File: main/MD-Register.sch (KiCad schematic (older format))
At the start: 19 parts, among them U68 74LS245, U69 74LS173, U70 74LS173

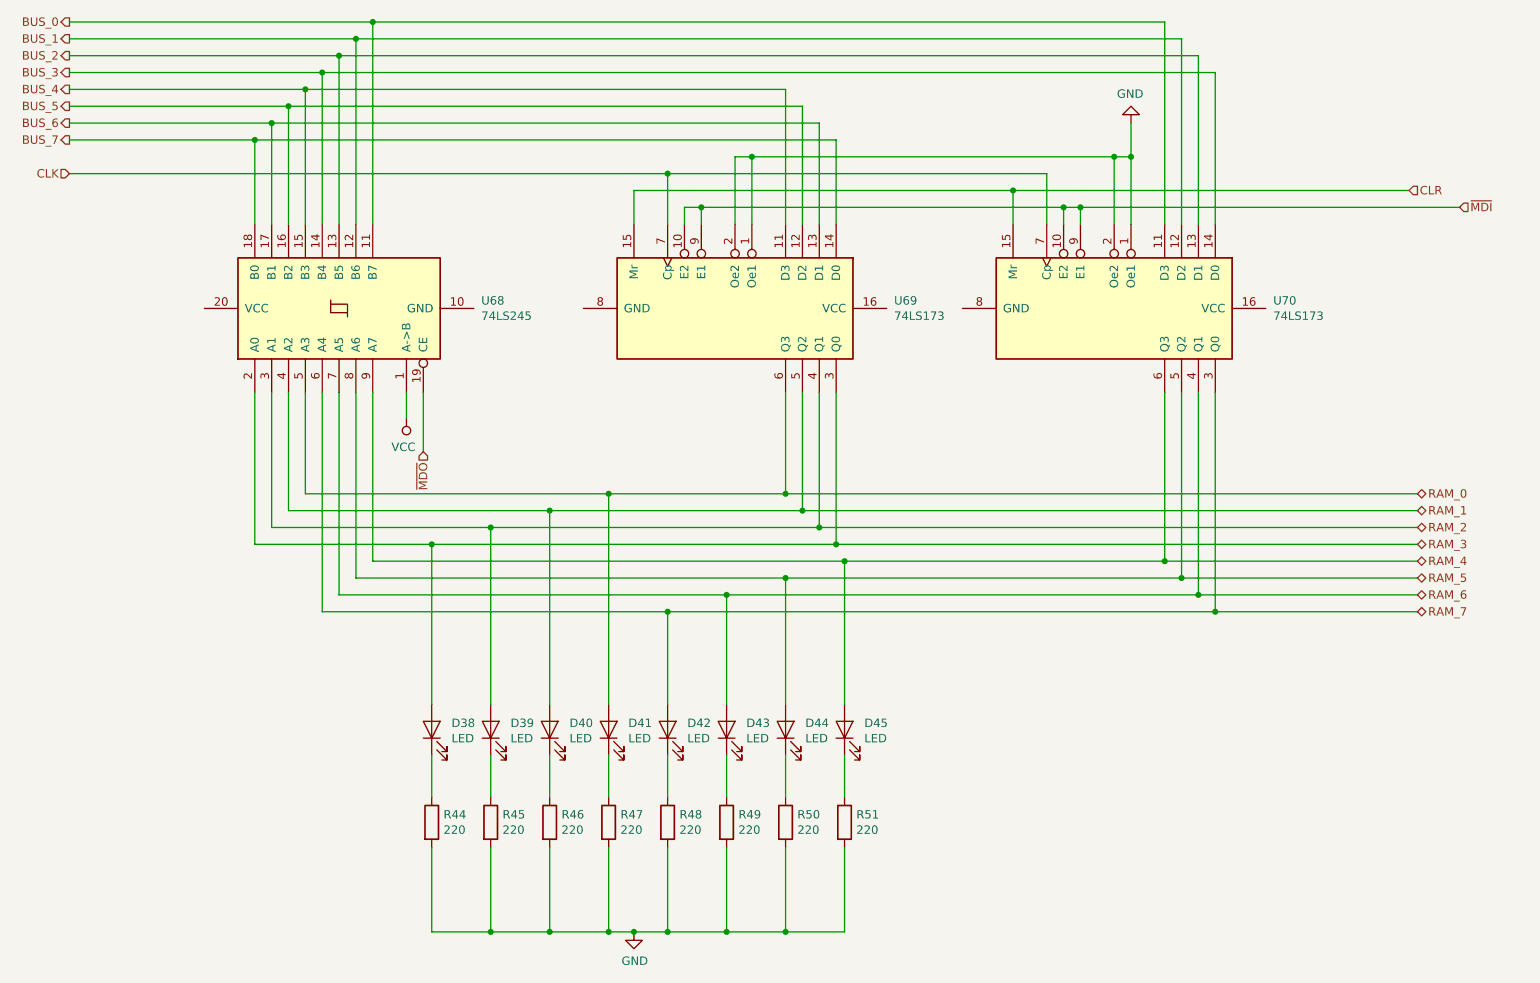
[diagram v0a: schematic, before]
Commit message: Replot main with symbols
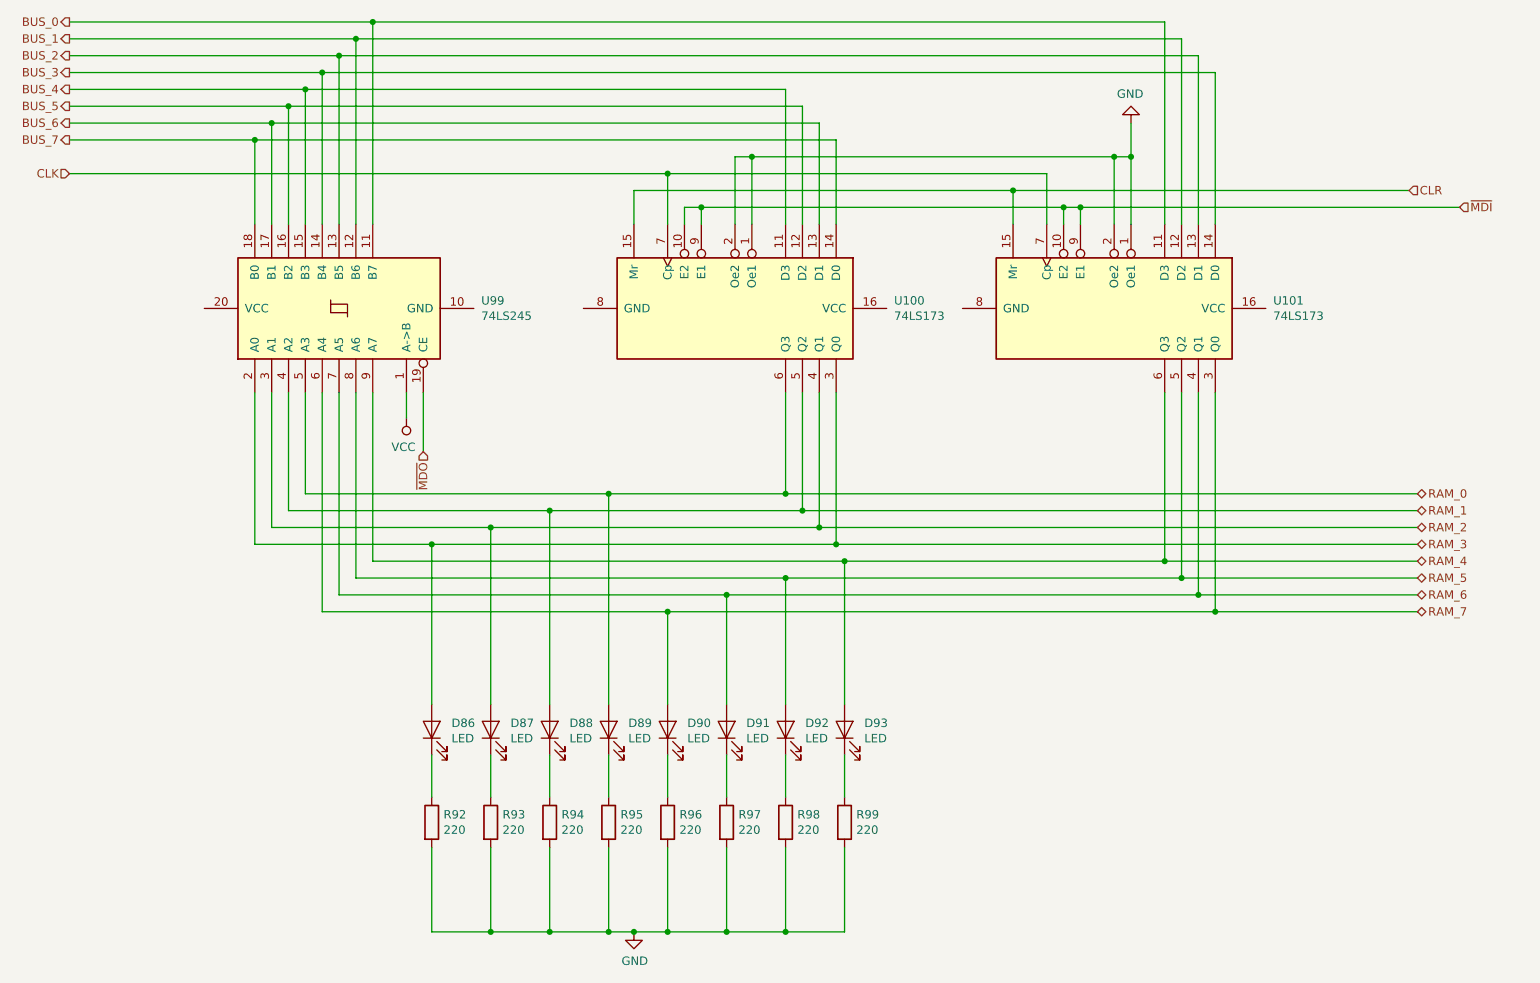
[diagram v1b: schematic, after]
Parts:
- renumbered D38 to D86, D39 to D87, D40 to D88, D41 to D89, D42 to D90, D43 to D91, D44 to D92, D45 to D93, R44 to R92, R45 to R93, R46 to R94, R47 to R95, R48 to R96, R49 to R97, R50 to R98, R51 to R99, U69 to U100, U70 to U101, U68 to U99
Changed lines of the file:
@@
 Sheet 26 26
 Title "Memory Data Register"
-Date "2019-11-13"
+Date "2019-11-17"
 Rev "v1.0"
 Comp "Christopher Milan"
@@
 AR Path="/5DA98D6D/5DA9A5B3/5E61466D" Ref="U?"  Part="1"
 AR Path="/5DA9B7A7/5E61466D" Ref="U?"  Part="1"
-AR Path="/5E5B2276/5D8079E9/5E61466D" Ref="U68"  Part="1"
-F 0 "U68" V 2746 2056 50  0000 R CNN
+AR Path="/5E5B2276/5D8079E9/5E61466D" Ref="U99"  Part="1"
+F 0 "U99" V 2746 2056 50  0000 R CNN
 F 1 "74LS245" V 2655 2056 50  0000 R CNN
 F 2 "" H 2700 2900 50  0001 C CNN
@@
 AR Path="/5DA98D6D/5DA9A5B3/5E61469A" Ref="U?"  Part="1"
 AR Path="/5DA9B7A7/5E61469A" Ref="U?"  Part="1"
-AR Path="/5E5B2276/5D8079E9/5E61469A" Ref="U70"  Part="1"
-F 0 "U70" V 7254 3844 50  0000 L CNN
+AR Path="/5E5B2276/5D8079E9/5E61469A" Ref="U101"  Part="1"
+F 0 "U101" V 7254 3844 50  0000 L CNN
 F 1 "74LS173" V 7345 3844 50  0000 L CNN
 F 2 "" H 7300 2900 50  0001 C CNN
@@
 AR Path="/5DA98D6D/5DA9A5B3/5E6146C4" Ref="D?"  Part="1"
 AR Path="/5DA9B7A7/5E6146C4" Ref="D?"  Part="1"
-AR Path="/5E5B2276/5D8079E9/5E6146C4" Ref="D38"  Part="1"
-F 0 "D38" V 3289 5283 50  0000 R CNN
+AR Path="/5E5B2276/5D8079E9/5E6146C4" Ref="D86"  Part="1"
+F 0 "D86" V 3289 5283 50  0000 R CNN
 F 1 "LED" V 3198 5283 50  0000 R CNN
 F 2 "" H 3250 5400 50  0001 C CNN
@@
 AR Path="/5DA98D6D/5DA9A5B3/5E6146CA" Ref="D?"  Part="1"
 AR Path="/5DA9B7A7/5E6146CA" Ref="D?"  Part="1"
-AR Path="/5E5B2276/5D8079E9/5E6146CA" Ref="D39"  Part="1"
-F 0 "D39" V 3639 5283 50  0000 R CNN
+AR Path="/5E5B2276/5D8079E9/5E6146CA" Ref="D87"  Part="1"
+F 0 "D87" V 3639 5283 50  0000 R CNN
 F 1 "LED" V 3548 5283 50  0000 R CNN
 F 2 "" H 3600 5400 50  0001 C CNN
@@
 AR Path="/5DA98D6D/5DA9A5B3/5E6146D0" Ref="D?"  Part="1"
 AR Path="/5DA9B7A7/5E6146D0" Ref="D?"  Part="1"
-AR Path="/5E5B2276/5D8079E9/5E6146D0" Ref="D40"  Part="1"
-F 0 "D40" V 3989 5283 50  0000 R CNN
+AR Path="/5E5B2276/5D8079E9/5E6146D0" Ref="D88"  Part="1"
+F 0 "D88" V 3989 5283 50  0000 R CNN
 F 1 "LED" V 3898 5283 50  0000 R CNN
 F 2 "" H 3950 5400 50  0001 C CNN
@@
 AR Path="/5DA98D6D/5DA9A5B3/5E6146D6" Ref="D?"  Part="1"
 AR Path="/5DA9B7A7/5E6146D6" Ref="D?"  Part="1"
-AR Path="/5E5B2276/5D8079E9/5E6146D6" Ref="D41"  Part="1"
-F 0 "D41" V 4339 5283 50  0000 R CNN
+AR Path="/5E5B2276/5D8079E9/5E6146D6" Ref="D89"  Part="1"
+F 0 "D89" V 4339 5283 50  0000 R CNN
 F 1 "LED" V 4248 5283 50  0000 R CNN
 F 2 "" H 4300 5400 50  0001 C CNN
@@
 AR Path="/5DA98D6D/5DA9A5B3/5E6146DC" Ref="D?"  Part="1"
 AR Path="/5DA9B7A7/5E6146DC" Ref="D?"  Part="1"
-AR Path="/5E5B2276/5D8079E9/5E6146DC" Ref="D42"  Part="1"
-F 0 "D42" V 4689 5283 50  0000 R CNN
+AR Path="/5E5B2276/5D8079E9/5E6146DC" Ref="D90"  Part="1"
+F 0 "D90" V 4689 5283 50  0000 R CNN
 F 1 "LED" V 4598 5283 50  0000 R CNN
 F 2 "" H 4650 5400 50  0001 C CNN
@@
 AR Path="/5DA98D6D/5DA9A5B3/5E6146E2" Ref="D?"  Part="1"
 AR Path="/5DA9B7A7/5E6146E2" Ref="D?"  Part="1"
-AR Path="/5E5B2276/5D8079E9/5E6146E2" Ref="D43"  Part="1"
-F 0 "D43" V 5039 5283 50  0000 R CNN
+AR Path="/5E5B2276/5D8079E9/5E6146E2" Ref="D91"  Part="1"
+F 0 "D91" V 5039 5283 50  0000 R CNN
 F 1 "LED" V 4948 5283 50  0000 R CNN
 F 2 "" H 5000 5400 50  0001 C CNN
@@
 AR Path="/5DA98D6D/5DA9A5B3/5E6146E8" Ref="D?"  Part="1"
 AR Path="/5DA9B7A7/5E6146E8" Ref="D?"  Part="1"
-AR Path="/5E5B2276/5D8079E9/5E6146E8" Ref="D44"  Part="1"
-F 0 "D44" V 5389 5283 50  0000 R CNN
+AR Path="/5E5B2276/5D8079E9/5E6146E8" Ref="D92"  Part="1"
+F 0 "D92" V 5389 5283 50  0000 R CNN
 F 1 "LED" V 5298 5283 50  0000 R CNN
 F 2 "" H 5350 5400 50  0001 C CNN
@@
 AR Path="/5DA98D6D/5DA9A5B3/5E6146EE" Ref="D?"  Part="1"
 AR Path="/5DA9B7A7/5E6146EE" Ref="D?"  Part="1"
-AR Path="/5E5B2276/5D8079E9/5E6146EE" Ref="D45"  Part="1"
-F 0 "D45" V 5739 5283 50  0000 R CNN
+AR Path="/5E5B2276/5D8079E9/5E6146EE" Ref="D93"  Part="1"
+F 0 "D93" V 5739 5283 50  0000 R CNN
 F 1 "LED" V 5648 5283 50  0000 R CNN
 F 2 "" H 5700 5400 50  0001 C CNN
@@
 AR Path="/5DA98D6D/5DA9A5B3/5E61470A" Ref="R?"  Part="1"
 AR Path="/5DA9B7A7/5E61470A" Ref="R?"  Part="1"
-AR Path="/5E5B2276/5D8079E9/5E61470A" Ref="R44"  Part="1"
-F 0 "R44" H 3320 5996 50  0000 L CNN
+AR Path="/5E5B2276/5D8079E9/5E61470A" Ref="R92"  Part="1"
+F 0 "R92" H 3320 5996 50  0000 L CNN
 F 1 "220" H 3320 5905 50  0000 L CNN
 F 2 "" V 3180 5950 50  0001 C CNN
@@
 AR Path="/5DA98D6D/5DA9A5B3/5E614710" Ref="R?"  Part="1"
 AR Path="/5DA9B7A7/5E614710" Ref="R?"  Part="1"
-AR Path="/5E5B2276/5D8079E9/5E614710" Ref="R45"  Part="1"
-F 0 "R45" H 3670 5996 50  0000 L CNN
+AR Path="/5E5B2276/5D8079E9/5E614710" Ref="R93"  Part="1"
+F 0 "R93" H 3670 5996 50  0000 L CNN
 F 1 "220" H 3670 5905 50  0000 L CNN
 F 2 "" V 3530 5950 50  0001 C CNN
@@
 AR Path="/5DA98D6D/5DA9A5B3/5E614716" Ref="R?"  Part="1"
 AR Path="/5DA9B7A7/5E614716" Ref="R?"  Part="1"
-AR Path="/5E5B2276/5D8079E9/5E614716" Ref="R46"  Part="1"
-F 0 "R46" H 4020 5996 50  0000 L CNN
+AR Path="/5E5B2276/5D8079E9/5E614716" Ref="R94"  Part="1"
+F 0 "R94" H 4020 5996 50  0000 L CNN
 F 1 "220" H 4020 5905 50  0000 L CNN
 F 2 "" V 3880 5950 50  0001 C CNN
@@
 AR Path="/5DA98D6D/5DA9A5B3/5E61471C" Ref="R?"  Part="1"
 AR Path="/5DA9B7A7/5E61471C" Ref="R?"  Part="1"
-AR Path="/5E5B2276/5D8079E9/5E61471C" Ref="R47"  Part="1"
-F 0 "R47" H 4370 5996 50  0000 L CNN
+AR Path="/5E5B2276/5D8079E9/5E61471C" Ref="R95"  Part="1"
+F 0 "R95" H 4370 5996 50  0000 L CNN
 F 1 "220" H 4370 5905 50  0000 L CNN
 F 2 "" V 4230 5950 50  0001 C CNN
@@
 AR Path="/5DA98D6D/5DA9A5B3/5E614722" Ref="R?"  Part="1"
 AR Path="/5DA9B7A7/5E614722" Ref="R?"  Part="1"
-AR Path="/5E5B2276/5D8079E9/5E614722" Ref="R48"  Part="1"
-F 0 "R48" H 4720 5996 50  0000 L CNN
+AR Path="/5E5B2276/5D8079E9/5E614722" Ref="R96"  Part="1"
+F 0 "R96" H 4720 5996 50  0000 L CNN
 F 1 "220" H 4720 5905 50  0000 L CNN
 F 2 "" V 4580 5950 50  0001 C CNN
@@
 AR Path="/5DA98D6D/5DA9A5B3/5E614728" Ref="R?"  Part="1"
 AR Path="/5DA9B7A7/5E614728" Ref="R?"  Part="1"
-AR Path="/5E5B2276/5D8079E9/5E614728" Ref="R49"  Part="1"
-F 0 "R49" H 5070 5996 50  0000 L CNN
+AR Path="/5E5B2276/5D8079E9/5E614728" Ref="R97"  Part="1"
+F 0 "R97" H 5070 5996 50  0000 L CNN
 F 1 "220" H 5070 5905 50  0000 L CNN
 F 2 "" V 4930 5950 50  0001 C CNN
@@
 AR Path="/5DA98D6D/5DA9A5B3/5E61472E" Ref="R?"  Part="1"
 AR Path="/5DA9B7A7/5E61472E" Ref="R?"  Part="1"
-AR Path="/5E5B2276/5D8079E9/5E61472E" Ref="R50"  Part="1"
-F 0 "R50" H 5420 5996 50  0000 L CNN
+AR Path="/5E5B2276/5D8079E9/5E61472E" Ref="R98"  Part="1"
+F 0 "R98" H 5420 5996 50  0000 L CNN
 F 1 "220" H 5420 5905 50  0000 L CNN
 F 2 "" V 5280 5950 50  0001 C CNN
@@
 AR Path="/5DA98D6D/5DA9A5B3/5E614734" Ref="R?"  Part="1"
 AR Path="/5DA9B7A7/5E614734" Ref="R?"  Part="1"
-AR Path="/5E5B2276/5D8079E9/5E614734" Ref="R51"  Part="1"
-F 0 "R51" H 5770 5996 50  0000 L CNN
+AR Path="/5E5B2276/5D8079E9/5E614734" Ref="R99"  Part="1"
+F 0 "R99" H 5770 5996 50  0000 L CNN
 F 1 "220" H 5770 5905 50  0000 L CNN
 F 2 "" V 5630 5950 50  0001 C CNN
@@
 AR Path="/5DA98D6D/5DA9A5B3/5E614785" Ref="U?"  Part="1"
 AR Path="/5DA9B7A7/5E614785" Ref="U?"  Part="1"
-AR Path="/5E5B2276/5D8079E9/5E614785" Ref="U69"  Part="1"
-F 0 "U69" V 5004 3844 50  0000 L CNN
+AR Path="/5E5B2276/5D8079E9/5E614785" Ref="U100"  Part="1"
+F 0 "U100" V 5004 3844 50  0000 L CNN
 F 1 "74LS173" V 5095 3844 50  0000 L CNN
 F 2 "" H 5050 2900 50  0001 C CNN

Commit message: Switch to using 74LS377 in place of two 74LS173
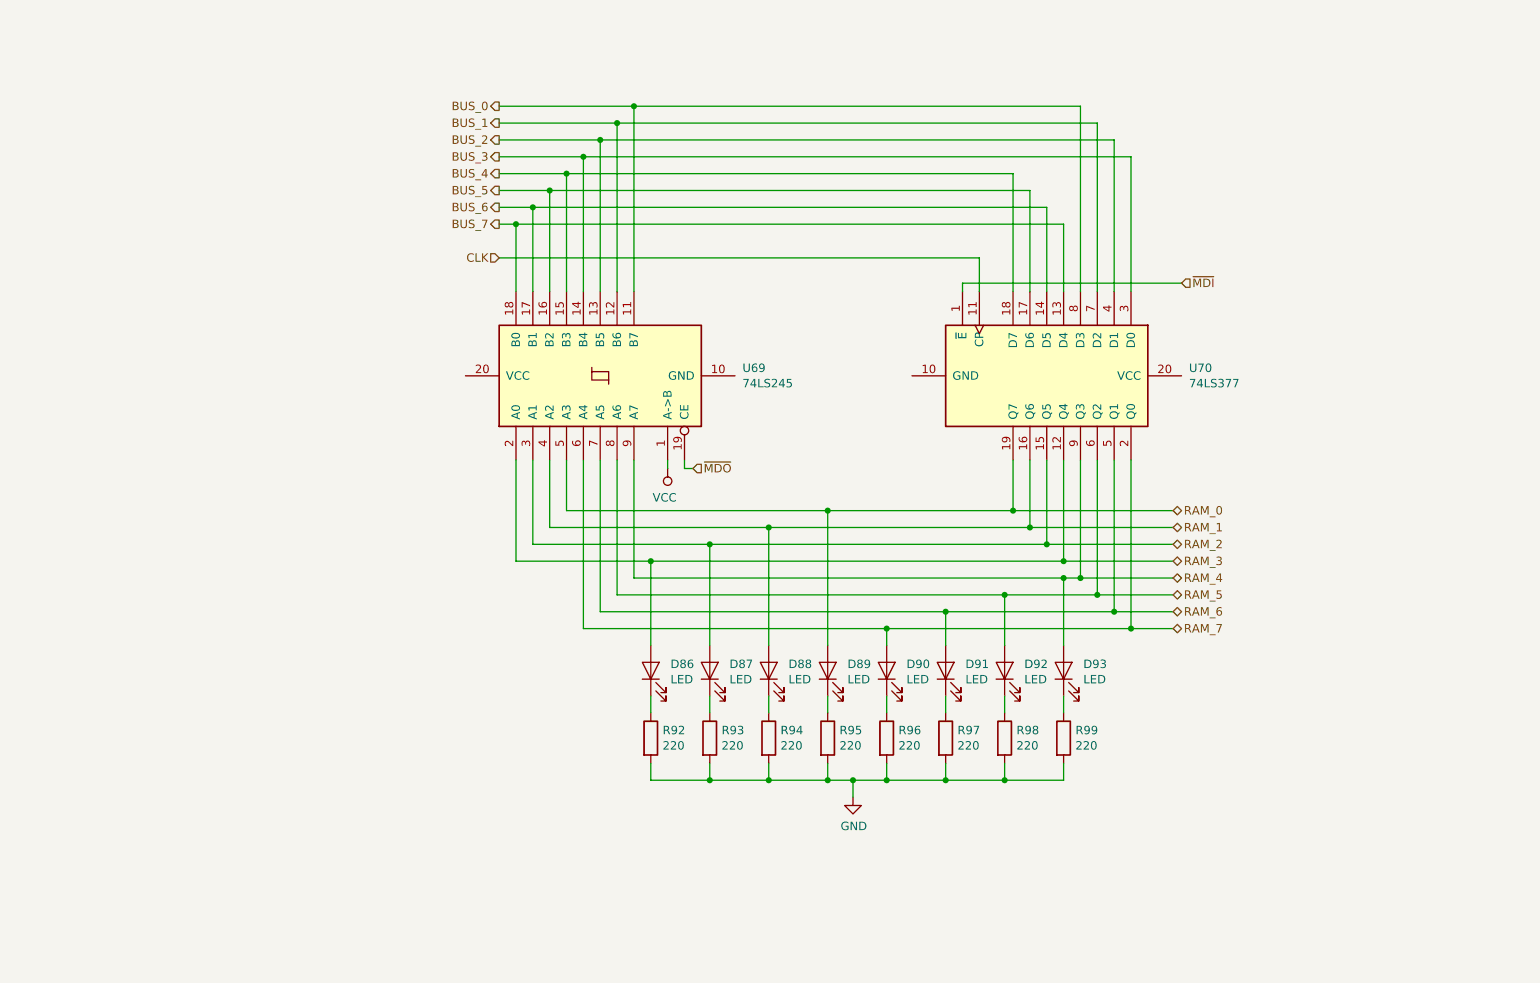
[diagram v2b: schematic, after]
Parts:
- removed U100, U101: 74LS173, symbol 74xx:74LS173
- removed U99: 74LS245, symbol 74xx:74LS245
- added U69: 74LS245, symbol 74xx:74LS245
- added U70: 74LS377, symbol 74xx:74LS377
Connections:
- net BUS_0: now also U69.11 (B7), U70.8 (D3)
- net BUS_1: now also U69.12 (B6), U70.7 (D2)
- net BUS_2: now also U69.13 (B5), U70.4 (D1)
- net BUS_3: now also U69.14 (B4), U70.3 (D0)
- net BUS_4: now also U69.15 (B3), U70.18 (D7)
- net BUS_5: now also U69.16 (B2), U70.17 (D6)
- net BUS_6: now also U69.17 (B1), U70.14 (D5)
- net BUS_7: now also U69.18 (B0), U70.13 (D4)
- net CLK: now also U70.11 (CP)
- net RAM_0: now also U69.5 (A3), U70.19 (Q7)
- net RAM_1: now also U69.4 (A2), U70.16 (Q6)
- net RAM_2: now also U69.3 (A1), U70.15 (Q5)
- net RAM_3: now also U69.2 (A0), U70.12 (Q4)
- net RAM_4: now also U69.9 (A7), U70.9 (Q3)
- net RAM_5: now also U69.8 (A6), U70.6 (Q2)
- net RAM_6: now also U69.7 (A5), U70.5 (Q1)
- net RAM_7: now also U69.6 (A4), U70.2 (Q0)
- net VCC: now also U69.1 (A->B)
- net ~MDI~: now also U70.1 (~E)
- net ~MDO~: now also U69.19 (CE)
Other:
- moved on the sheet: D86, D87, D88, D89, D90, D91, D92, D93, R92, R93, R94, R95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
